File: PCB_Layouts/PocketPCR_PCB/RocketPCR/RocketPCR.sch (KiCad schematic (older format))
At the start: 50 parts, among them J1 Conn_01x02_Male, J2 Conn_02x05_Odd_Even, J3 USB_C_Receptacle, Q1 Q_NMOS_GSD, Q2 Q_NMOS_GSD, Q3 Q_NMOS_GSD, SW1 Rotary_Encoder_Switch, U1 TLV1117-33, U2 SAMD21G18B-A changed from SAM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, X1 PAD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

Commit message: New Version with Bottom Heater Improved software
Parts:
- removed D1: DIODE, Diode_SMD:D_1210_3225Metric, symbol pspice:DIODE
- removed L1: L, Inductor_SMD:L_1206_3216Metric, symbol Device:L
- added C13: 100nF, Capacitor_SMD:C_0805_2012Metric, symbol RocketPCR-rescue:C
- added R6: 4.7k, Resistor_SMD:R_0805_2012Metric, symbol RocketPCR-rescue:R
- added X12, X13: PAD, GaudiLabsFootPrints:SolderPad1_8mm, symbol GaudiLabsPartsLibrary:PAD
- C3: footprint Capacitor_SMD:C_1206_3216Metric -> GaudiLabsFootPrints:C_2512_HandSoldering
- J3: footprint Connectors_USB:USB_C_Receptacle_Amphenol_12401610E4-2A -> GaudiLabsFootPrints:USB_C_Receptacle_Amphenol_12401610E4-2A
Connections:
- net +3V3: now also C13.2, R6.2
- net +5V: now also C3.1, J1.2 (Pin_2), X1.1, X4.1
- net GND: now also C13.1, X13.1
- net AC renamed TEMP_LID
- net TEMP_LID: now also R6.1, X12.1
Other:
- moved on the sheet: R4, X3, X6
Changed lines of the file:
@@
 TEMP_BLOCK
 Text GLabel 7800 5300 2    60   Input ~ 0
-AC
+TEMP_LID
 Text GLabel 7800 3600 2    60   Input ~ 0
 POL
@@
 F 0 "C3" H 2575 7700 50  0000 L CNN
 F 1 "22uF" H 2575 7500 50  0000 L CNN
-F 2 "Capacitor_SMD:C_1206_3216Metric" H 2588 7450 30  0001 C CNN
+F 2 "GaudiLabsFootPrints:C_2512_HandSoldering" H 2588 7450 30  0001 C CNN
 F 3 "" H 2550 7600 60  0000 C CNN
 	1    2550 7600
@@
 F 0 "J3" H 12350 8900 50  0000 L CNN
 F 1 "USB_C_Receptacle" H 13150 8900 50  0000 R CNN
-F 2 "Connectors_USB:USB_C_Receptacle_Amphenol_12401610E4-2A" H 12900 7450 50  0001 C CNN
+F 2 "GaudiLabsFootPrints:USB_C_Receptacle_Amphenol_12401610E4-2A" H 12900 7450 50  0001 C CNN
 F 3 "" H 12900 7450 50  0001 C CNN
 	1    12750 7450
@@
 Wire Wire Line
 	7750 7150 7750 7300
-Text GLabel 10300 6100 2    60   Input ~ 0
+Text GLabel 9950 6150 2    60   Input ~ 0
 TEMP_BLOCK
 $Comp
 L RocketPCR-rescue:GND #PWR0105
 U 1 1 5D0DDB77
-P 10100 6650
-F 0 "#PWR0105" H 10100 6400 50  0001 C CNN
-F 1 "GND" H 10100 6500 50  0000 C CNN
-F 2 "" H 10100 6650 60  0000 C CNN
-F 3 "" H 10100 6650 60  0000 C CNN
-	1    10100 6650
+P 9750 6700
+F 0 "#PWR0105" H 9750 6450 50  0001 C CNN
+F 1 "GND" H 9750 6550 50  0000 C CNN
+F 2 "" H 9750 6700 60  0000 C CNN
+F 3 "" H 9750 6700 60  0000 C CNN
+	1    9750 6700
 	1    0    0    -1
 $EndComp
@@
 L RocketPCR-rescue:+3V3 #PWR0106
 U 1 1 5D0DDEB6
-P 10100 5550
-F 0 "#PWR0106" H 10100 5400 50  0001 C CNN
-F 1 "+3V3" H 10115 5723 50  0000 C CNN
-F 2 "" H 10100 5550 50  0001 C CNN
-F 3 "" H 10100 5550 50  0001 C CNN
-	1    10100 5550
+P 9750 5600
+F 0 "#PWR0106" H 9750 5450 50  0001 C CNN
+F 1 "+3V3" H 9765 5773 50  0000 C CNN
+F 2 "" H 9750 5600 50  0001 C CNN
+F 3 "" H 9750 5600 50  0001 C CNN
+	1    9750 5600
 	1    0    0    -1
 $EndComp
@@
 L RocketPCR-rescue:R R4
 U 1 1 5D0DDF65
-P 10100 5850
-F 0 "R4" V 10000 5850 50  0000 C CNN
-F 1 "4.7k" V 10200 5850 50  0000 C CNN
-F 2 "Resistor_SMD:R_0805_2012Metric" V 10030 5850 30  0001 C CNN
-F 3 "" H 10100 5850 30  0000 C CNN
-	1    10100 5850
+P 9750 5900
+F 0 "R4" V 9650 5900 50  0000 C CNN
+F 1 "4.7k" V 9850 5900 50  0000 C CNN
+F 2 "Resistor_SMD:R_0805_2012Metric" V 9680 5900 30  0001 C CNN
+F 3 "" H 9750 5900 30  0000 C CNN
+	1    9750 5900
 	-1   0    0    1
 $EndComp
 Wire Wire Line
-	10100 5550 10100 5700
-Wire Wire Line
-	10100 6000 10100 6100
-Wire Wire Line
-	10100 6100 10300 6100
-Connection ~ 10100 6100
-Wire Wire Line
-	10100 6100 10100 6200
-Wire Wire Line
-	10100 6500 10100 6650
+	9750 5600 9750 5750
+Wire Wire Line
+	9750 6050 9750 6150
+Wire Wire Line
+	9750 6150 9950 6150
+Connection ~ 9750 6150
+Wire Wire Line
+	9750 6150 9750 6250
+Wire Wire Line
+	9750 6550 9750 6700
 $Comp
 L GaudiLabsPartsLibrary:PAD X3
 U 1 1 5D18C80F
-P 10100 6300
-F 0 "X3" V 10050 6550 60  0000 L CNN
-F 1 "PAD" V 10150 6500 60  0000 L CNN
-F 2 "GaudiLabsFootPrints:SolderPad1_8mm" H 10100 6300 60  0001 C CNN
-F 3 "" H 10100 6300 60  0001 C CNN
-	1    10100 6300
+P 9750 6350
+F 0 "X3" V 9700 6600 60  0000 L CNN
+F 1 "PAD" V 9800 6550 60  0000 L CNN
+F 2 "GaudiLabsFootPrints:SolderPad1_8mm" H 9750 6350 60  0001 C CNN
+F 3 "" H 9750 6350 60  0001 C CNN
+	1    9750 6350
 	0    1    1    0
 $EndComp
@@
 L GaudiLabsPartsLibrary:PAD X6
 U 1 1 5D18C8E5
-P 10100 6400
-F 0 "X6" V 10050 6650 60  0000 L CNN
-F 1 "PAD" V 9900 6700 60  0000 L CNN
-F 2 "GaudiLabsFootPrints:SolderPad1_8mm" H 10100 6400 60  0001 C CNN
-F 3 "" H 10100 6400 60  0001 C CNN
-	1    10100 6400
+P 9750 6450
+F 0 "X6" V 9700 6700 60  0000 L CNN
+F 1 "PAD" V 9550 6750 60  0000 L CNN
+F 2 "GaudiLabsFootPrints:SolderPad1_8mm" H 9750 6450 60  0001 C CNN
+F 3 "" H 9750 6450 60  0001 C CNN
+	1    9750 6450
 	0    -1   -1   0
 $EndComp
@@
 	0    1    1    0
 $EndComp
-$Comp
-L Device:L L1
-U 1 1 5D0DC543
-P 2200 7150
-F 0 "L1" V 2022 7150 50  0000 C CNN
-F 1 "L" V 2113 7150 50  0000 C CNN
-F 2 "Inductor_SMD:L_1206_3216Metric" H 2200 7150 50  0001 C CNN
-F 3 "~" H 2200 7150 50  0001 C CNN
-	1    2200 7150
-	0    1    1    0
-$EndComp
-Wire Wire Line
-	2050 7150 1900 7150
-Wire Wire Line
-	2350 7150 2550 7150
 Connection ~ 2550 7150
 Wire Wire Line
@@
 Wire Wire Line
 	2550 7150 2550 7450
-Wire Wire Line
-	2550 7750 2550 8250
 $Comp
 L RocketPCR-rescue:R R5
@@
 	10000 2200 10150 2200
 $Comp
-L pspice:DIODE D1
-U 1 1 5D15F83F
-P 1900 7800
-F 0 "D1" V 1946 7672 50  0000 R CNN
-F 1 "DIODE" V 1855 7672 50  0000 R CNN
-F 2 "Diode_SMD:D_1210_3225Metric" H 1900 7800 50  0001 C CNN
-F 3 "~" H 1900 7800 50  0001 C CNN
-	1    1900 7800
-	0    -1   -1   0
-$EndComp
-Wire Wire Line
-	1900 7600 1900 7150
-Connection ~ 1900 7150
-Wire Wire Line
-	1900 7150 1600 7150
-Wire Wire Line
-	1900 8000 1900 8250
-Wire Wire Line
-	1900 8250 2550 8250
-Connection ~ 2550 8250
-Wire Wire Line
-	2550 8250 2550 8400
-$Comp
 L GaudiLabsPartsLibrary:PAD X8
 U 1 1 5D182149
@@
 	1    0    0    -1
 $EndComp
+Text GLabel 10900 6150 2    60   Input ~ 0
+TEMP_LID
+$Comp
+L RocketPCR-rescue:GND #PWR0107
+U 1 1 5DCCB246
+P 10700 6700
+F 0 "#PWR0107" H 10700 6450 50  0001 C CNN
+F 1 "GND" H 10700 6550 50  0000 C CNN
+F 2 "" H 10700 6700 60  0000 C CNN
+F 3 "" H 10700 6700 60  0000 C CNN
+	1    10700 6700
+	1    0    0    -1
+$EndComp
+$Comp
+L RocketPCR-rescue:+3V3 #PWR0108
+U 1 1 5DCCB24C
+P 10700 5600
+F 0 "#PWR0108" H 10700 5450 50  0001 C CNN
+F 1 "+3V3" H 10715 5773 50  0000 C CNN
+F 2 "" H 10700 5600 50  0001 C CNN
+F 3 "" H 10700 5600 50  0001 C CNN
+	1    10700 5600
+	1    0    0    -1
+$EndComp
+$Comp
+L RocketPCR-rescue:R R6
+U 1 1 5DCCB252
+P 10700 5900
+F 0 "R6" V 10600 5900 50  0000 C CNN
+F 1 "4.7k" V 10800 5900 50  0000 C CNN
+F 2 "Resistor_SMD:R_0805_2012Metric" V 10630 5900 30  0001 C CNN
+F 3 "" H 10700 5900 30  0000 C CNN
+	1    10700 5900
+	-1   0    0    1
+$EndComp
+Wire Wire Line
+	10700 5600 10700 5750
+Wire Wire Line
+	10700 6050 10700 6150
+Wire Wire Line
+	10700 6150 10900 6150
+Connection ~ 10700 6150
+Wire Wire Line
+	10700 6150 10700 6250
+Wire Wire Line
+	10700 6550 10700 6700
+$Comp
+L GaudiLabsPartsLibrary:PAD X12
+U 1 1 5DCCB25E
+P 10700 6350
+F 0 "X12" V 10650 6600 60  0000 L CNN
+F 1 "PAD" V 10750 6550 60  0000 L CNN
+F 2 "GaudiLabsFootPrints:SolderPad1_8mm" H 10700 6350 60  0001 C CNN
+F 3 "" H 10700 6350 60  0001 C CNN
+	1    10700 6350
+	0    1    1    0
+$EndComp
+$Comp
+L GaudiLabsPartsLibrary:PAD X13
+U 1 1 5DCCB264
+P 10700 6450
+F 0 "X13" V 10650 6700 60  0000 L CNN
+F 1 "PAD" V 10500 6750 60  0000 L CNN
+F 2 "GaudiLabsFootPrints:SolderPad1_8mm" H 10700 6450 60  0001 C CNN
+F 3 "" H 10700 6450 60  0001 C CNN
+	1    10700 6450
+	0    -1   -1   0
+$EndComp
+$Comp
+L RocketPCR-rescue:C C13
+U 1 1 5DD03848
+P 5950 9900
+F 0 "C13" H 5800 9800 50  0000 L CNN
+F 1 "100nF" H 5750 10000 50  0000 L CNN
+F 2 "Capacitor_SMD:C_0805_2012Metric" H 5988 9750 30  0001 C CNN
+F 3 "" H 5950 9900 60  0000 C CNN
+	1    5950 9900
+	-1   0    0    1
+$EndComp
+Wire Wire Line
+	5650 9500 5950 9500
+Wire Wire Line
+	5950 9500 5950 9750
+Wire Wire Line
+	5950 10050 5950 10200
+Wire Wire Line
+	5950 10200 5650 10200
+Wire Wire Line
+	2550 7750 2550 8400
+Wire Wire Line
+	1600 7150 2550 7150
 $EndSCHEMATC

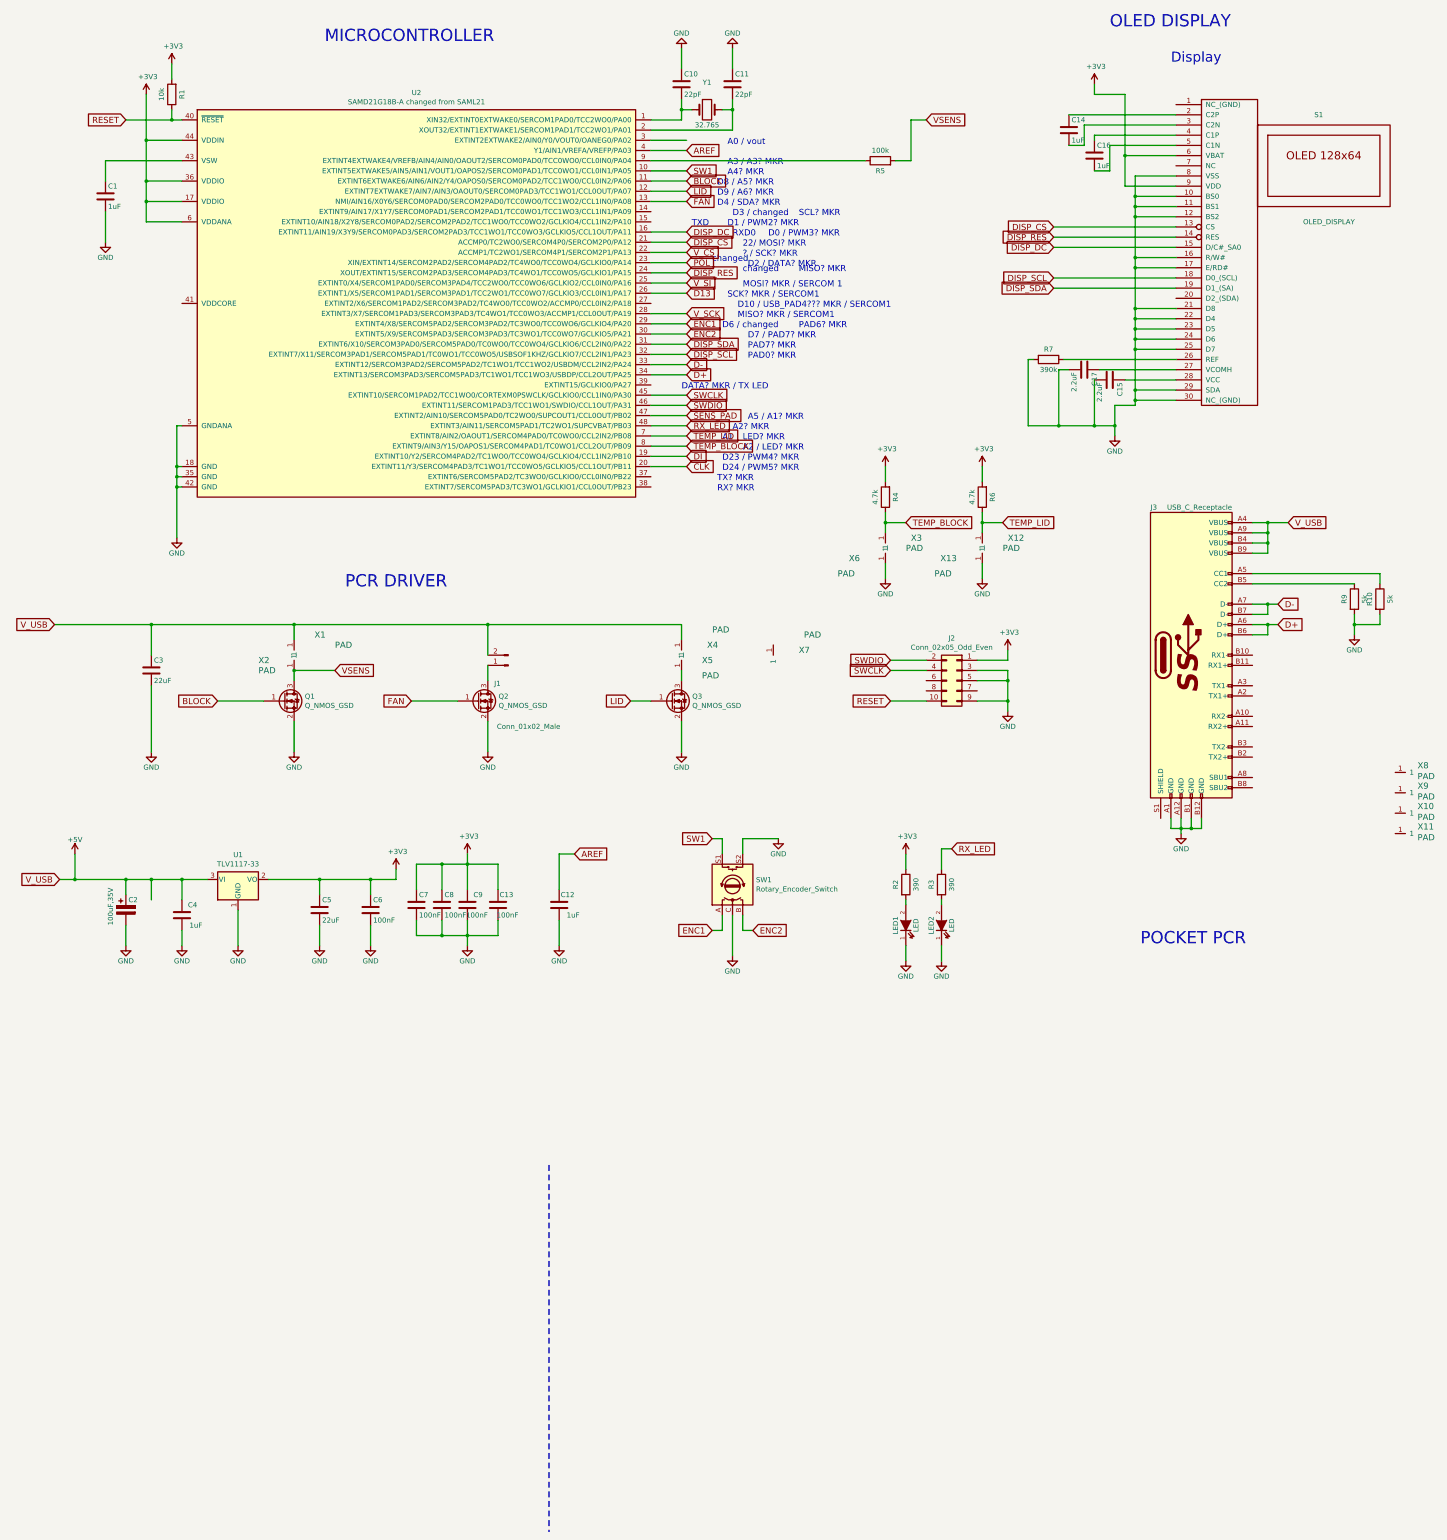
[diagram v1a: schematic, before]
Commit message: Updated PCB, BOM, added Heater Hardware
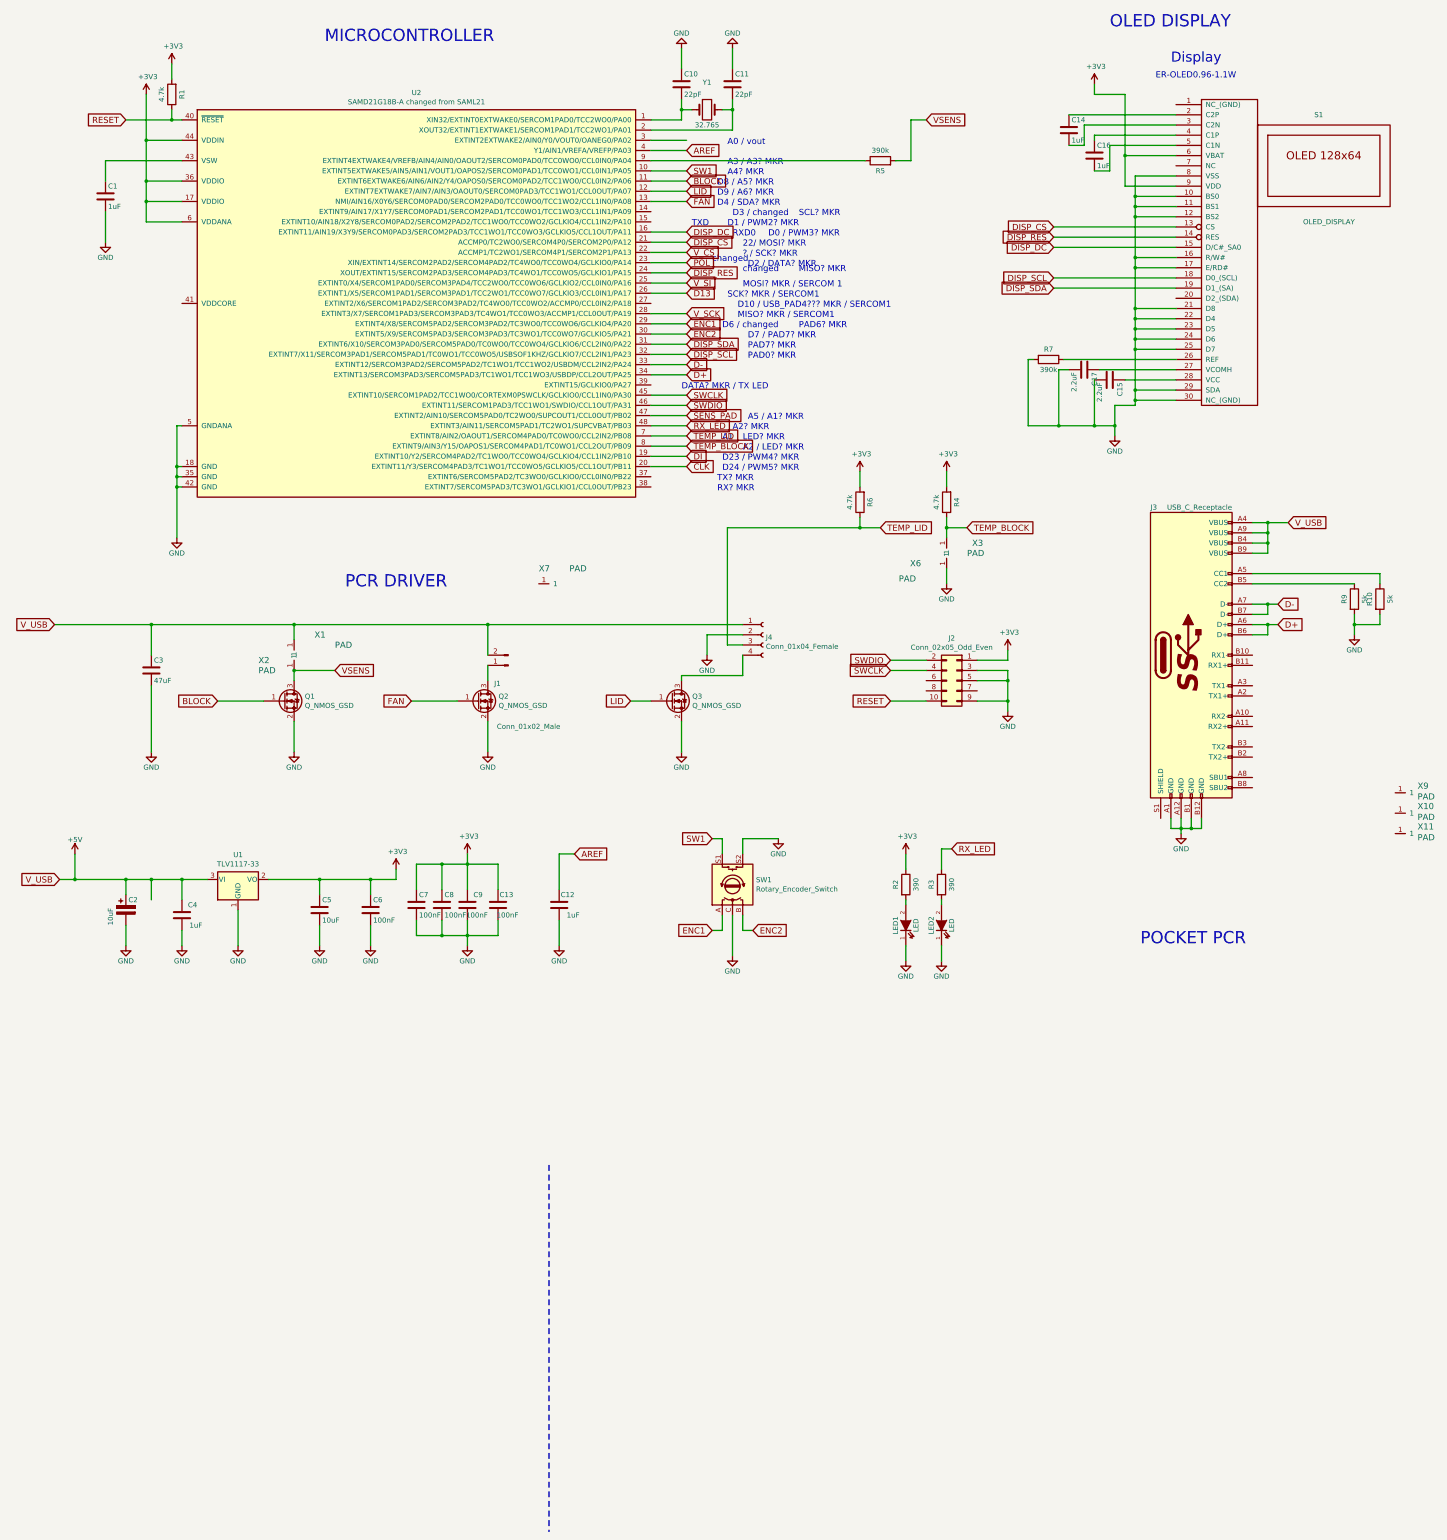
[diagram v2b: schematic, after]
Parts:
- removed X12, X13, X4, X5: PAD, GaudiLabsFootPrints:SolderPad1_8mm, symbol GaudiLabsPartsLibrary:PAD
- removed X8: PAD, GaudiLabsFootPrints:Fiducial_Cooper, symbol GaudiLabsPartsLibrary:PAD
- added J4: Conn_01x04_Female, Connector_JST:JST_XH_S04B-XH-A_1x04_P2.50mm_Horizontal, symbol Connector:Conn_01x04_Female
- C2: value 100uF,35V -> 10uF
- C3: value 22uF -> 47uF; footprint GaudiLabsFootPrints:C_2512_HandSoldering -> Capacitor_SMD:C_1206_3216Metric_Pad1.42x1.75mm_HandSolder
- C5: value 22uF -> 10uF
- J1: footprint Connector_PinHeader_2.54mm:PinHeader_1x02_P2.54mm_Vertical -> GaudiLabsFootPrints:PinHeader_JST_1x02_P2.54mm_Vertical
- R1: value 10k -> 4.7k
- R5: value 100k -> 390k
- X10, X11, X9: footprint GaudiLabsFootPrints:Fiducial_Cooper -> GaudiLabsFootPrints:Fiducial_1mm_Dia_2.54mm_Outer_CopperBottom
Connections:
- net +5V: now also J4.1 (Pin_1)
- net GND: now also J4.2 (Pin_2)
- net TEMP_LID: now also J4.3 (Pin_3)
- net at Q3.3 (D): now also J4.4 (Pin_4)
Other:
- note added: "ER-OLED0.96-1.1W"
- moved on the sheet: R4, R6, X3, X6, X7
